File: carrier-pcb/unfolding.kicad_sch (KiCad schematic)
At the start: 82 parts, among them J1 USB4125-GF-A_REVA, J2 Conn_01x01_Female, J3 1-338068-8, J4 Conn_01x01_Female, J5 Conn_01x01_Female, J6 Conn_01x01_Female, J7 Fan, U1 TCA9548APWR, U10 DRV2605LDGS, U11 DRV2605LDGS, U12 LSM6DSxx, U13 WE 82400102, U14 MMC5633NJL, U2 TCA9548APWR, U3 DRV2605LDGS, U4 DRV2605LDGS, U5 DRV2605LDGS, U6 DRV2605LDGS, U7 DRV2605LDGS, U8 DRV2605LDGS, U9 DRV2605LDGS

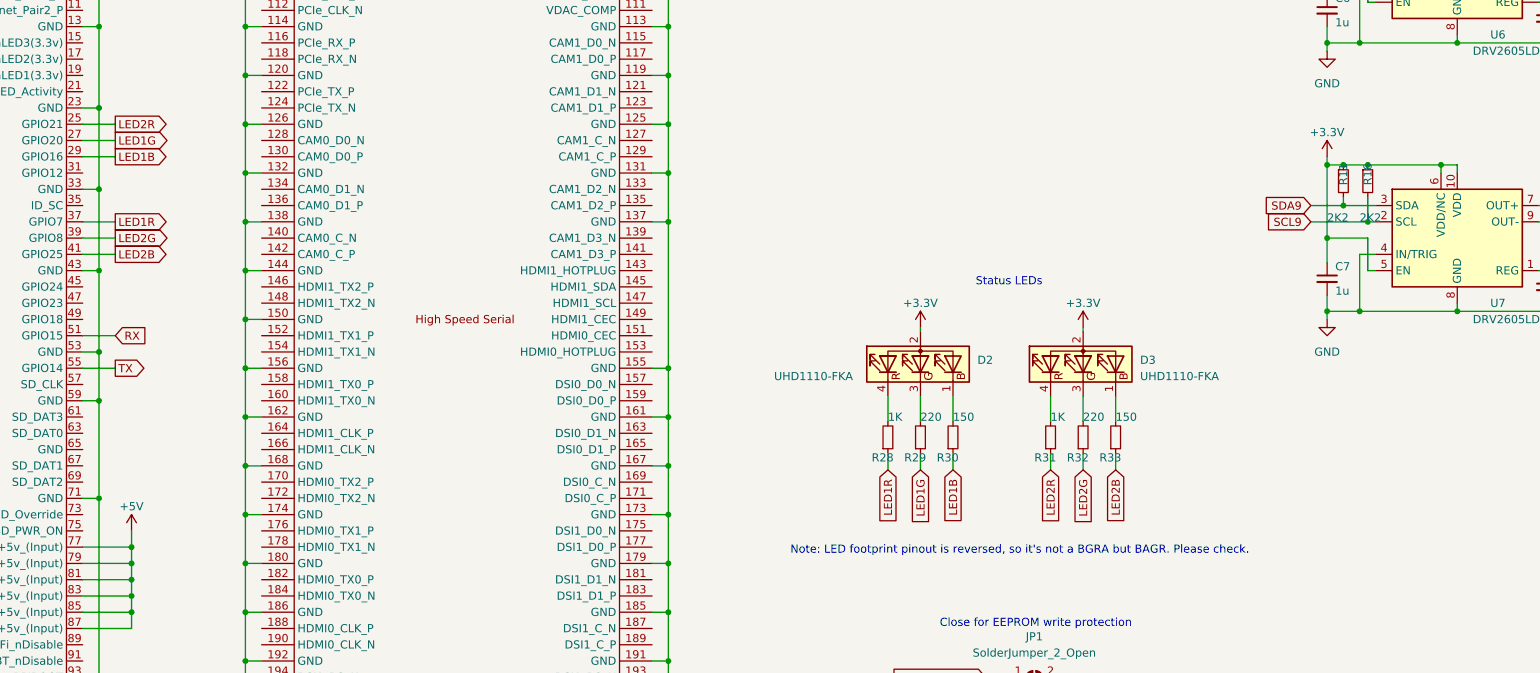
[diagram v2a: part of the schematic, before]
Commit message: Changed RGB LED footprints
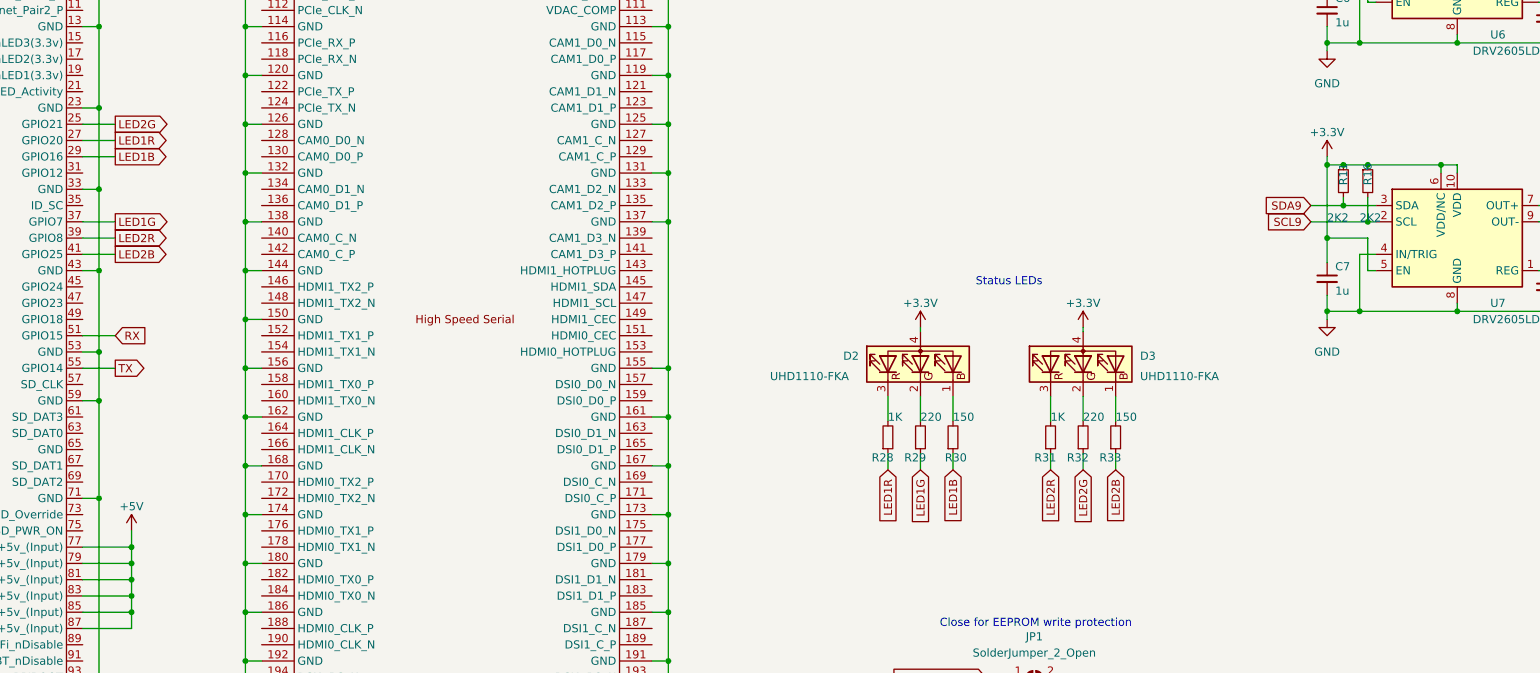
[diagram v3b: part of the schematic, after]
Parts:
- removed D2, D3: UHD1110-FKA, LED_SMD:LED_Lumex_SML-LX0404SIUPGUSB, symbol Device:LED_BAGR
- added D2, D3: UHD1110-FKA, RGBLED:UHD1110-FKA, symbol Device:LED_BGRA
- R28: renamed from R29; value 220 -> 1K
- R29: renamed from R28; value 1K -> 220
- R31: renamed from R32; value 220 -> 1K
- R32: renamed from R31; value 1K -> 220
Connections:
- net +3V3: now also D2.4 (A), D3.4 (A)
- net LED1G: now also Module1.37 (GPIO7), R29.1; no longer Module1.27 (GPIO20), R28.1
- net LED1R: now also Module1.27 (GPIO20), R28.1; no longer Module1.37 (GPIO7), R29.1
- net LED2G: now also Module1.25 (GPIO21), R32.1; no longer Module1.39 (GPIO8), R31.1
- net LED2R: now also Module1.39 (GPIO8), R31.1; no longer Module1.25 (GPIO21), R32.1
- net at R30.2: now also D2.1 (BK)
- net at R29.2: now also D2.2 (GK)
- net at R33.2: now also D3.1 (BK)
- net at R31.2: now also D3.3 (RK)
- net at R32.2: now also D3.2 (GK)
- net at R28.2: now also D2.3 (RK)
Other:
- note removed: "Note: LED footprint pinout is reversed, so it's not a BGRA but BAGR. Please check."
- moved on the sheet: R28, R29, R31, R32
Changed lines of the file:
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@@
     (effects (font (size 1.27 1.27)) (justify right bottom))
   )
-  (text "Note: LED footprint pinout is reversed, so it's not a BGRA but BAGR. Please check."
-    (at 204.47 248.92 0)
-    (effects (font (size 1.27 1.27)) (justify left bottom))
-  )
   (text "Status LEDs" (at 243.84 207.01 180)
     (effects (font (size 1.27 1.27)) (justify right bottom))
@@
     )
   )
-  (global_label "LED2R" (shape output) (at 99.06 181.61 0) (fields_autoplaced)
+  (global_label "LED2G" (shape output) (at 99.06 181.61 0) (fields_autoplaced)
     (effects (font (size 1.27 1.27)) (justify left))
     (property "Intersheet References" "${INTERSHEET_REFS}" (id 0) (at 107.3998 181.5306 0)
@@
     )
   )
-  (global_label "LED1G" (shape output) (at 99.06 184.15 0) (fields_autoplaced)
+  (global_label "LED1R" (shape output) (at 99.06 184.15 0) (fields_autoplaced)
     (effects (font (size 1.27 1.27)) (justify left))
     (property "Intersheet References" "${INTERSHEET_REFS}" (id 0) (at 107.3998 184.0706 0)
@@
     )
   )
-  (global_label "LED1R" (shape output) (at 99.06 196.85 0) (fields_autoplaced)
+  (global_label "LED1G" (shape output) (at 99.06 196.85 0) (fields_autoplaced)
     (effects (font (size 1.27 1.27)) (justify left))
     (property "Intersheet References" "${INTERSHEET_REFS}" (id 0) (at 107.3998 196.7706 0)
@@
     )
   )
-  (global_label "LED2G" (shape output) (at 99.06 199.39 0) (fields_autoplaced)
+  (global_label "LED2R" (shape output) (at 99.06 199.39 0) (fields_autoplaced)
     (effects (font (size 1.27 1.27)) (justify left))
     (property "Intersheet References" "${INTERSHEET_REFS}" (id 0) (at 107.3998 199.3106 0)
@@
   (symbol (lib_id "Device:R_Small") (at 229.87 230.505 0) (mirror x) (unit 1)
     (in_bom yes) (on_board yes)
-    (property "Reference" "R30" (id 0) (at 227.33 233.6801 0)
+    (property "Reference" "R30" (id 0) (at 228.6 233.6801 0)
       (effects (font (size 1.27 1.27)) (justify left))
     )
@@
     (pin "2")
   )
-  (symbol (lib_id "Device:LED_BAGR") (at 224.79 219.075 90) (unit 1)
+  (symbol (lib_id "Device:LED_BGRA") (at 224.79 219.075 90) (unit 1)
     (in_bom yes) (on_board yes)
-    (property "Reference" "D2" (id 0) (at 233.68 218.4399 90)
+    (property "Reference" "D2" (id 0) (at 212.725 217.8049 90)
       (effects (font (size 1.27 1.27)) (justify right))
     )
-    (property "Value" "UHD1110-FKA" (id 1) (at 201.93 220.9799 90)
+    (property "Value" "UHD1110-FKA" (id 1) (at 201.295 220.9799 90)
       (effects (font (size 1.27 1.27)) (justify right))
     )
-    (property "Footprint" "LED_SMD:LED_Lumex_SML-LX0404SIUPGUSB" (id 2) (at 226.06 219.075 0)
+    (property "Footprint" "RGBLED:UHD1110-FKA" (id 2) (at 226.06 219.075 0)
       (effects (font (size 1.27 1.27)) hide)
     )
@@
     (pin "4")
   )
-  (symbol (lib_id "Device:LED_BAGR") (at 250.19 219.075 90) (unit 1)
-    (in_bom yes) (on_board yes) (fields_autoplaced)
-    (property "Reference" "D3" (id 0) (at 259.08 218.4399 90)
+  (symbol (lib_id "Device:LED_BGRA") (at 250.19 219.075 90) (unit 1)
+    (in_bom yes) (on_board yes)
+    (property "Reference" "D3" (id 0) (at 259.08 217.8049 90)
       (effects (font (size 1.27 1.27)) (justify right))
     )
@@
       (effects (font (size 1.27 1.27)) (justify right))
     )
-    (property "Footprint" "LED_SMD:LED_Lumex_SML-LX0404SIUPGUSB" (id 2) (at 251.46 219.075 0)
+    (property "Footprint" "RGBLED:UHD1110-FKA" (id 2) (at 251.46 219.075 0)
       (effects (font (size 1.27 1.27)) hide)
     )
@@
       (reference "D1") (unit 1) (value "SMBJ5.0A") (footprint "Diode_SMD:D_SMA")
     )
-    (path "/ca2be125-353b-4672-9538-ae2020bd963d"
-      (reference "D2") (unit 1) (value "UHD1110-FKA") (footprint "LED_SMD:LED_Lumex_SML-LX0404SIUPGUSB")
+    (path "/be694c2f-0b69-463f-af65-6a1dd3d86cea"
+      (reference "D2") (unit 1) (value "UHD1110-FKA") (footprint "RGBLED:UHD1110-FKA")
     )
-    (path "/1a60e1fc-8e57-4de2-af5c-2688606d208b"
-      (reference "D3") (unit 1) (value "UHD1110-FKA") (footprint "LED_SMD:LED_Lumex_SML-LX0404SIUPGUSB")
+    (path "/e9ae074d-884e-420d-bd86-35e90eb7d964"
+      (reference "D3") (unit 1) (value "UHD1110-FKA") (footprint "RGBLED:UHD1110-FKA")
     )
     (path "/07e1e970-2cb6-491a-bec9-3bb9395c712b"
@@
       (reference "R26") (unit 1) (value "2K2") (footprint "Resistor_SMD:R_0603_1608Metric")
     )
-    (path "/10461fa0-580f-4b6d-b18e-cc9f2ab3f21c"
+    (path "/c11daecf-b37c-45f2-ab4a-1ad70b0d756f"
       (reference "R28") (unit 1) (value "1K") (footprint "Resistor_SMD:R_0603_1608Metric")
     )
-    (path "/c11daecf-b37c-45f2-ab4a-1ad70b0d756f"
+    (path "/10461fa0-580f-4b6d-b18e-cc9f2ab3f21c"
       (reference "R29") (unit 1) (value "220") (footprint "Resistor_SMD:R_0603_1608Metric")
     )
@@
       (reference "R30") (unit 1) (value "150") (footprint "Resistor_SMD:R_0603_1608Metric")
     )
-    (path "/8c78953e-5609-44af-bf48-371b803cd098"
+    (path "/73a0f840-4599-4a24-badb-e8662e0714cd"
       (reference "R31") (unit 1) (value "1K") (footprint "Resistor_SMD:R_0603_1608Metric")
     )
-    (path "/73a0f840-4599-4a24-badb-e8662e0714cd"
+    (path "/8c78953e-5609-44af-bf48-371b803cd098"
       (reference "R32") (unit 1) (value "220") (footprint "Resistor_SMD:R_0603_1608Metric")
     )
